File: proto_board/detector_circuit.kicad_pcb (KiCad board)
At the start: 4 copper layers, 94 x 99.1 mm, 135 parts, among them J1 Programming Header, J10 Conn_01x06_Female, J3 BATT_1, J4 BATT_2, J5 BATT_3, J6 BATT_4, J7 TEST_CONN, J8 693072010801, J9 SIPM_CONN, Q1 BSS138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

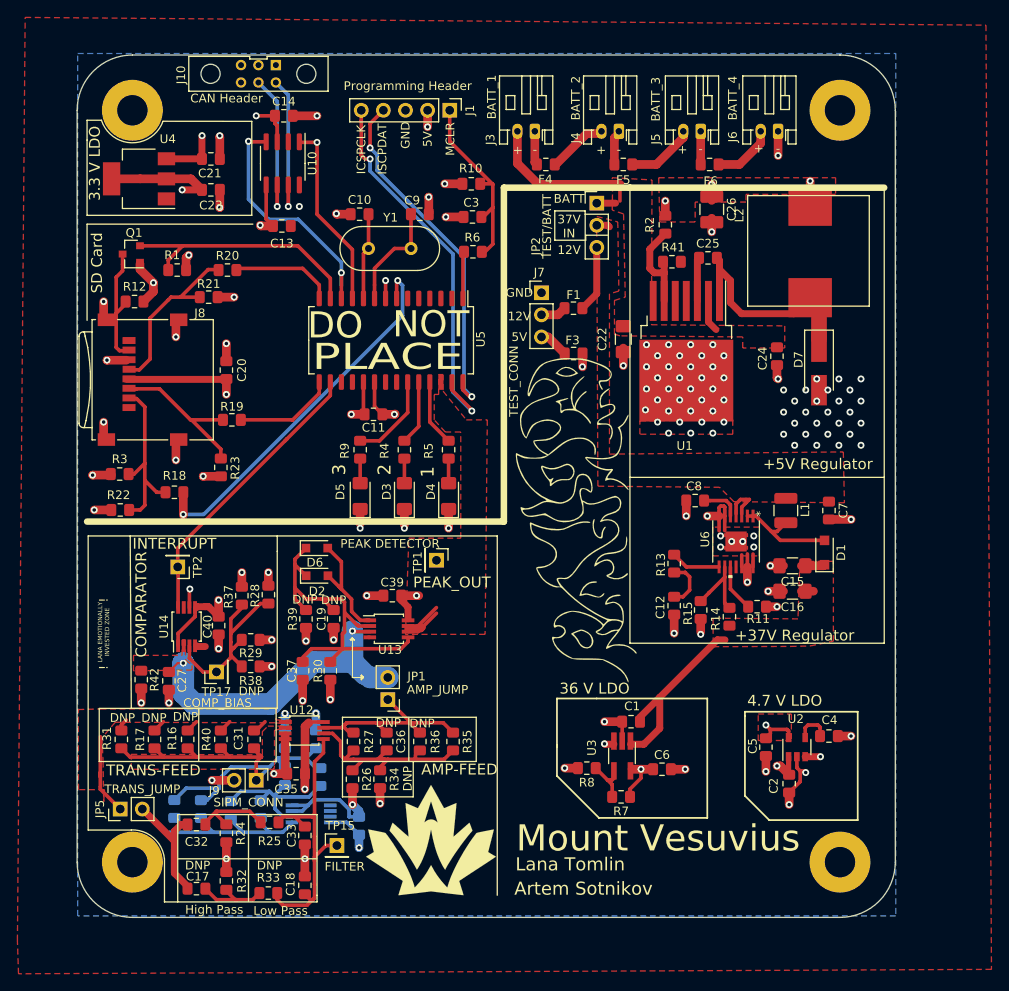
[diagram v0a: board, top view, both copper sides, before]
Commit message: addressed zach and Jared's reviews
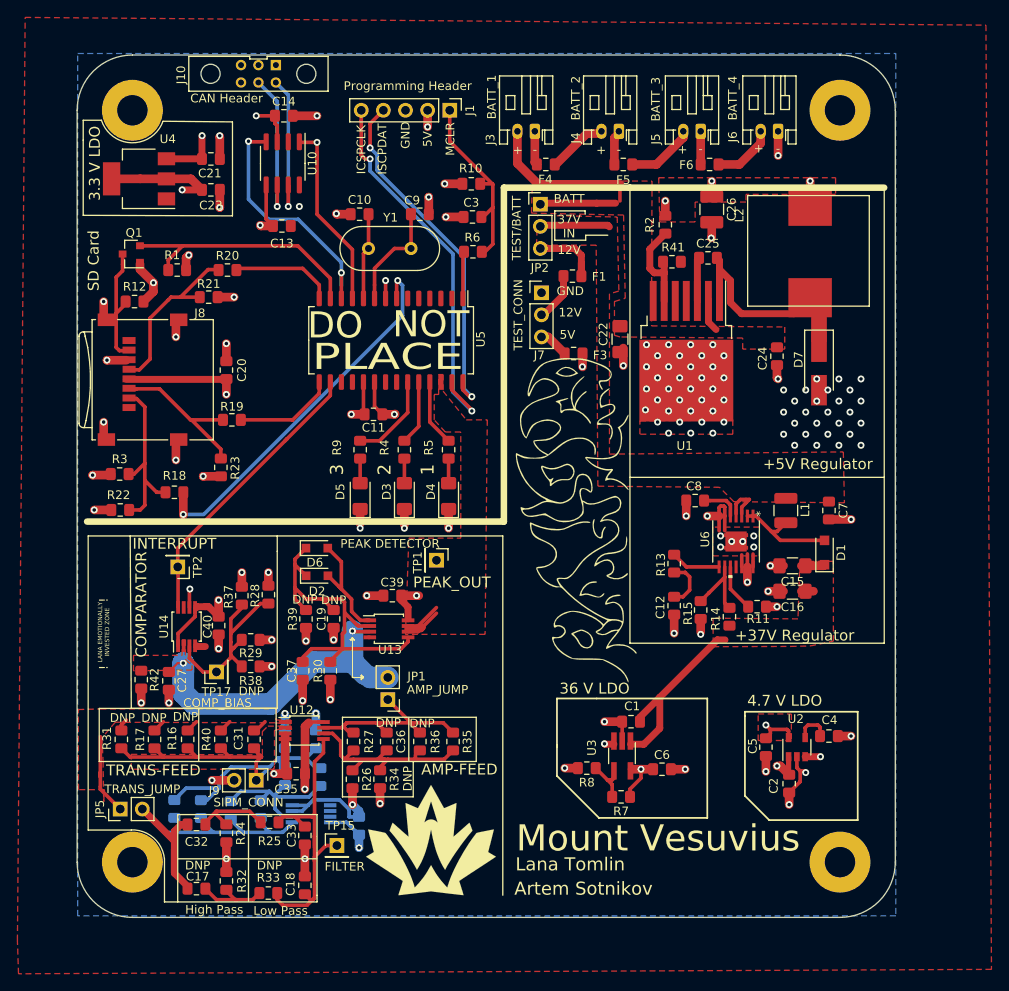
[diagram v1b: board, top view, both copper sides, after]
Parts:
- moved JP2 6.48 mm to (137.0, 65.4)
- moved F1 3.68 mm to (140.7, 73.7)
- moved C22 0.38 mm to (146.2, 80.9)
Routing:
- net Net-(C7-Pad1): track 6.41 -> 12.9 mm
- net +BATT: track 25.1 -> 31.7 mm
- net Net-(F1-Pad2): track 2.96 -> 5.63 mm
- net +12V: track 7.67 -> 9.14 mm

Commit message: made silkscreen less ugly
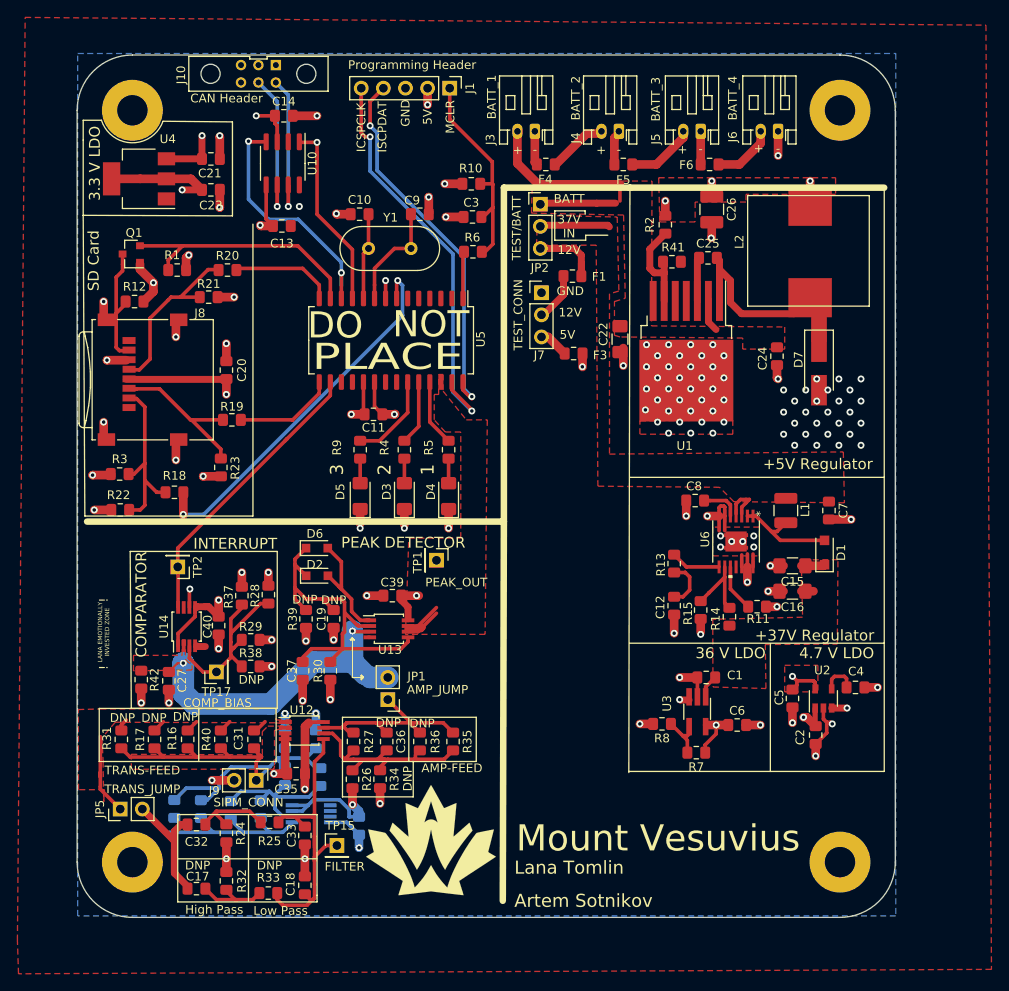
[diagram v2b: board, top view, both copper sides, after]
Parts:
- removed the G*** at (141.5, 101.5)
- C30, R43, R45: value DNP -> 0
- moved C6 10.0 mm to (159.6, 125.2)
- moved R7 10.0 mm to (154.9, 128.4)
- moved R8 10.0 mm to (151.0, 125.1)
- moved C1 10.0 mm to (156.1, 119.8)
- moved U3 10.0 mm to (155.1, 123.7)
- moved C4 6.37 mm to (173.2, 120.9)
- moved C2 6.37 mm to (168.7, 126.4)
- moved C5 6.37 mm to (166.0, 122.2)
- moved U2 6.37 mm to (169.5, 122.2)
- moved J1 2.54 mm to (126.6, 52.1)
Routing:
- net +37V: track 25.7 -> 6.78 mm
- net +36V: track 64.3 -> 78.0 mm
- net +4.7V: track 85.6 -> 78.5 mm
- net /Microcontroller [DO NOT PLACE]/MCLR: track 22.1 -> 24.7 mm
- net /Microcontroller [DO NOT PLACE]/ICSPDAT: track 40.7 -> 43.3 mm
- net /Microcontroller [DO NOT PLACE]/ICSPCLK: track 44.3 -> 46.8 mm

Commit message: finished layout for testing infastructure, now detatchable from detector circuit for easy swappability
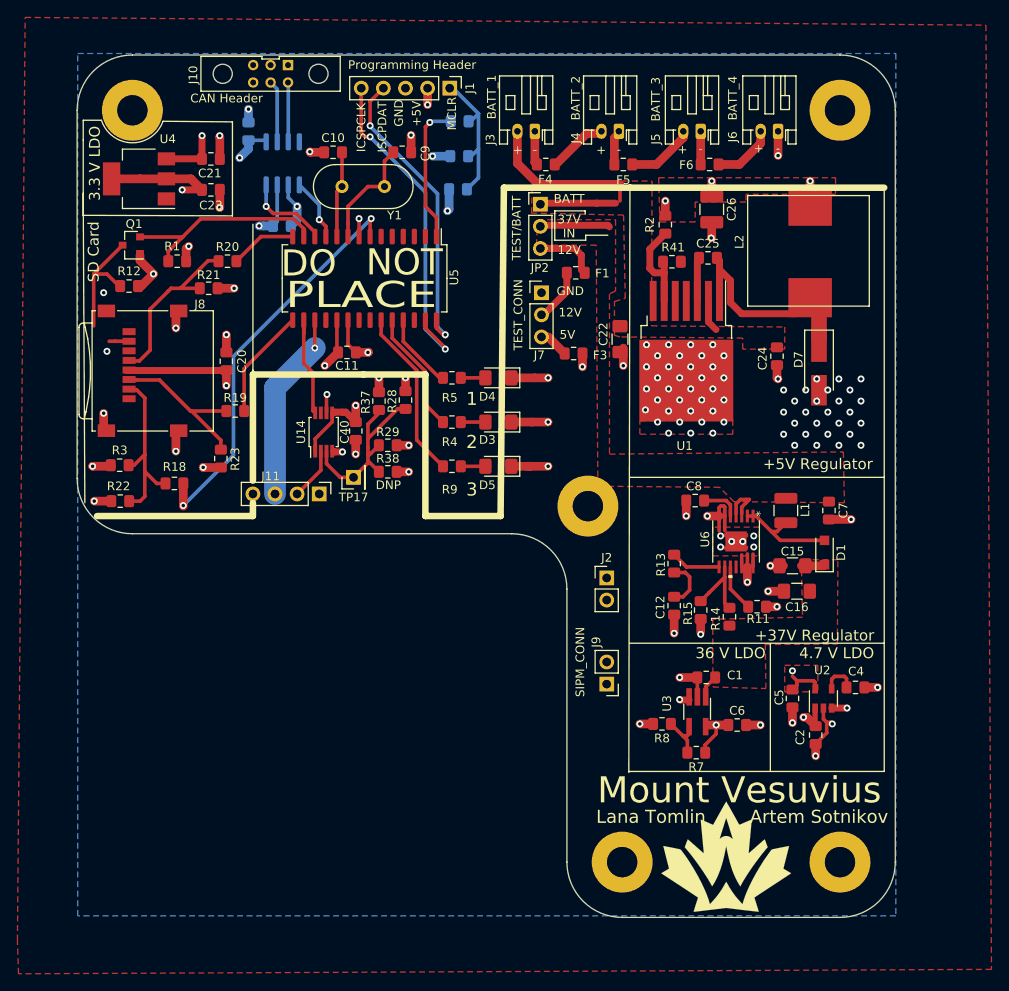
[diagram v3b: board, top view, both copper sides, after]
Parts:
- removed C17, C18, C19: DNP, Capacitor_SMD:C_0805_2012Metric_Pad1.15x1.40mm_HandSolder
- removed C27, C37: 2.2n, Capacitor_SMD:C_0805_2012Metric_Pad1.15x1.40mm_HandSolder
- removed C28, C29, C38: C, Capacitor_SMD:C_0805_2012Metric_Pad1.15x1.40mm_HandSolder
- removed C30: 0, Capacitor_SMD:C_0805_2012Metric_Pad1.15x1.40mm_HandSolder
- removed C31, C33, C34: 1n, Capacitor_SMD:C_0805_2012Metric_Pad1.15x1.40mm_HandSolder
- removed C32: 10n, Capacitor_SMD:C_0805_2012Metric_Pad1.15x1.40mm_HandSolder
- removed C35, C39: 0.1u, Capacitor_SMD:C_0805_2012Metric_Pad1.15x1.40mm_HandSolder
- removed C36: 470p, Capacitor_SMD:C_0805_2012Metric_Pad1.15x1.40mm_HandSolder
- removed D2, D6: CUS08F30H3FCT-ND, Diode_SMD:D_SOD-323_HandSoldering
- removed JP1: AMP_JUMP, Connector_PinHeader_2.54mm:PinHeader_1x02_P2.54mm_Vertical
- removed JP5: TRANS_JUMP, Connector_PinHeader_2.54mm:PinHeader_1x02_P2.54mm_Vertical
- removed R16, R17, R31, R32, R33, R34, R35, R36, R39: DNP, Resistor_SMD:R_0805_2012Metric_Pad1.15x1.40mm_HandSolder
- removed R24, R26: 100, Resistor_SMD:R_0805_2012Metric_Pad1.15x1.40mm_HandSolder
- removed R25, R40: 150, Resistor_SMD:R_0805_2012Metric_Pad1.15x1.40mm_HandSolder
- removed R27: 330, Resistor_SMD:R_0805_2012Metric_Pad1.15x1.40mm_HandSolder
- removed R30, R42: 1M, Resistor_SMD:R_0805_2012Metric_Pad1.15x1.40mm_HandSolder
- removed R43, R45: 0, Resistor_SMD:R_0805_2012Metric_Pad1.15x1.40mm_HandSolder
- removed R44, R46: 1k, Resistor_SMD:R_0805_2012Metric_Pad1.15x1.40mm_HandSolder
- removed TP1: PEAK_OUT, Connector_PinHeader_2.54mm:PinHeader_1x01_P2.54mm_Vertical
- removed TP15: FILTER, Connector_PinHeader_2.54mm:PinHeader_1x01_P2.54mm_Vertical
- removed TP2: INTERRUPT, Connector_PinHeader_2.54mm:PinHeader_1x01_P2.54mm_Vertical
- removed U12, U13, U7: LTC6269, Package_SO:MSOP-8_3x3mm_P0.65mm
- added J11: DET_CONN, Connector_PinHeader_2.54mm:PinHeader_1x04_P2.54mm_Vertical, F.Cu at (111.6, 98.7)
- added J2: DET_CONN_PWR, Connector_PinHeader_2.54mm:PinHeader_1x02_P2.54mm_Vertical, F.Cu at (144.7, 108.3)
- added REF**: MountingHole_3.5mm_Pad, MountingHole:MountingHole_3.5mm_Pad, F.Cu at (146.4, 141.0)
- C13, C14, C3, R10, R6, U10: moved to B.Cu
- moved REF** 66.4 mm to (142.5, 100.1)
- moved J9 41.7 mm to (144.7, 120.5), turned to 180 degrees
- moved G*** 34.0 mm to (158.4, 140.3)
- moved C40 27.3 mm to (115.8, 91.4)
- moved R28 27.3 mm to (121.5, 87.9)
- moved R29 27.3 mm to (119.5, 93.1)
- moved R37 27.3 mm to (118.5, 88.0)
- moved R38 27.3 mm to (119.5, 96.1)
- moved U14 27.3 mm to (112.1, 91.6)
- moved TP17 27.3 mm to (115.6, 96.8)
- moved D5 16.2 mm to (132.2, 95.5), turned to 180 degrees
- moved R6 15.1 mm to (127.8, 55.9)
- moved D4 14.7 mm to (132.2, 85.3), turned to 180 degrees
- moved D3 13.7 mm to (132.2, 90.4), turned to 180 degrees
- moved R9 10.7 mm to (126.9, 95.5), turned to 0 degrees
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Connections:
- C40 pad 1: +4.7V -> +5V
- R28 pad 1: +4.7V -> +5V
- R37 pad 1: +4.7V -> +5V
- U14 pad 1: +4.7V -> +5V
- U14 pad 5: +4.7V -> +5V
- U5 pad 17: (no net) -> /DET_ADC
- U5 pad 26: /DET_ADC -> (no net)
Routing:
- net +36V: track 78.0 -> 22.5 mm, vias 2 -> 1
- net /SIPM_OUT: track 54.3 -> 0.00 mm
- net +4.7V: track 78.5 -> 29.6 mm, vias 7 -> 1
- net /Filter_IN: track 45.2 -> 0.00 mm
- net /AMP_OUT: track 49.1 -> 6.04 mm, vias 2 -> 0
- net Net-(C19-Pad1): track 42.5 -> 0.00 mm
- net GND: track 157.1 -> 116.7 mm, vias 127 -> 114
- net Net-(C18-Pad2): track 36.8 -> 0.00 mm
- net Net-(C36-Pad2): track 25.8 -> 0.00 mm
- net Net-(C36-Pad1): track 24.5 -> 0.00 mm
- net /INTERUPT_OUT: track 33.5 -> 11.8 mm
- net Net-(C30-Pad2): track 18.5 -> 0.00 mm
- net /Microcontroller [DO NOT PLACE]/PIC_RX: track 28.1 -> 9.79 mm, vias 2 -> 1
- net Net-(C31-Pad1): track 17.3 -> 0.00 mm
- net /Microcontroller [DO NOT PLACE]/PIC_TX: track 22.3 -> 7.20 mm
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- removed copper zone on VCC.Cu, net +4.7V
- removed copper zone on F.Cu, net /AMP_OUT
- removed copper zone on F.Cu, net /DET_ADC
- removed copper zone on F.Cu, net /SIPM_OUT
- removed copper zone on F.Cu, net Net-(C31-Pad1)
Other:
- outline, holes or cut-outs redrawn
- board text added: "+5V"
- board text removed: "!"
- board text removed: "AMP-FEED"
- board text removed: "COMPARATOR"
- board text removed: "High Pass"
- board text removed: "LANA EMOTIONALLY INVESTED ZONE"
- board text removed: "Low Pass"
- board text removed: "PEAK DETECTOR"
- board text removed: "TRANS-FEED"
